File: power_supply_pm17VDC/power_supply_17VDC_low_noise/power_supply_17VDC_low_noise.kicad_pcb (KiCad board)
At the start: 2 copper layers, 87.9 x 95 mm, 36 parts, among them J1 Terminal_01x03, J2 Terminal_01x04, U1 LM317, U2 LM337, U3 LM7812, U4 LM7805

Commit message: agregando imagenes y pdf
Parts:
- moved C5 29.6 mm to (144.1, 91.6)
- moved D5 29.6 mm to (157.3, 93.5)
- moved R4 29.6 mm to (140.1, 131.8)
- moved R6 29.6 mm to (154.3, 102.1)
- moved RV1 29.6 mm to (150.8, 124.1)
- moved RV2 29.6 mm to (139.5, 92.0)
- moved U1 29.6 mm to (135.3, 102.5)
- moved U2 29.6 mm to (135.3, 124.1)
- moved U3 29.6 mm to (135.3, 76.1)
- moved C1 29.6 mm to (114.8, 98.3)
- moved C11 29.6 mm to (133.8, 56.4)
- moved C12 29.6 mm to (137.7, 64.6)
- moved C2 29.6 mm to (113.8, 125.7)
- moved C3 29.6 mm to (125.6, 97.1)
- moved C4 29.6 mm to (124.2, 116.5)
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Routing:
- net GND: track 392.8 -> 395.5 mm
- net Net-(D8-A): track 11.0 -> 13.1 mm
- net Net-(D2-K): track 71.8 -> 72.8 mm

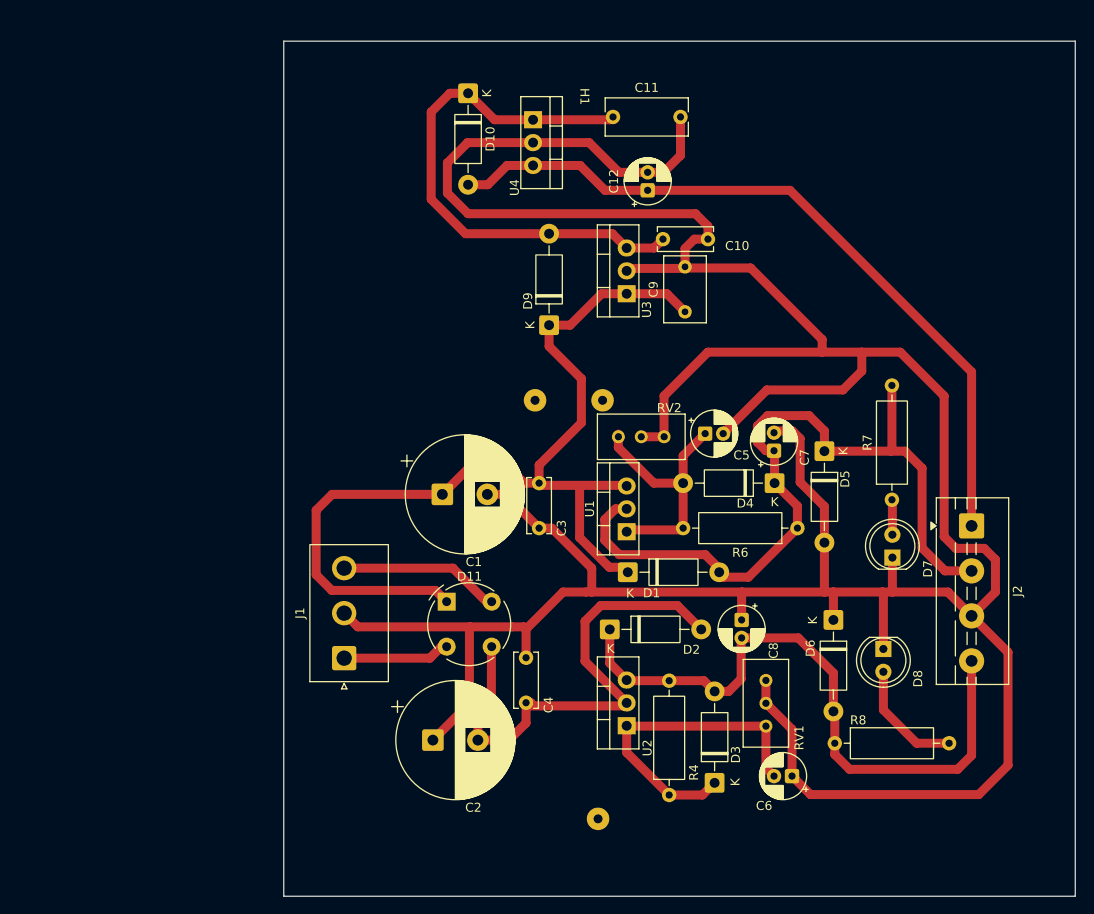
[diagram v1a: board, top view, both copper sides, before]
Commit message: finalizado STM y fuente de poder limpia, todo conforme a las huellas.
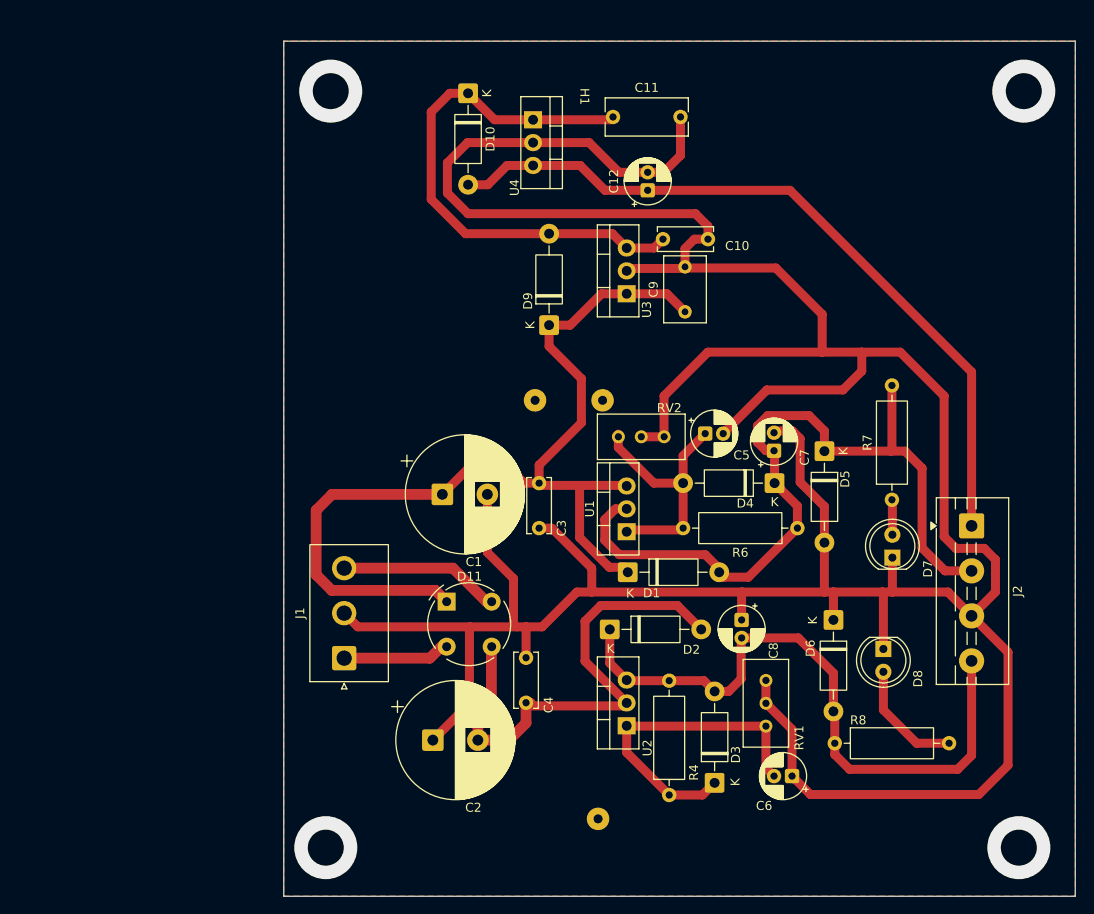
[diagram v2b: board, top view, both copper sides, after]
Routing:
- net GND: track 395.5 -> 405.5 mm
- net (no net): vias 0 -> 4
- added copper zone on F.Cu, net GND
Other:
- board text added: "mDamian 02/2026"
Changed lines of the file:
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@@
 		(layer "Margin")
+	)
+	(gr_text "mDamian 02/2026\n\n"
+		(at 105.3 84.1 0)
+		(layer "B.SilkS")
+		(effects
+			(font
+				(size 1 1)
+				(thickness 0.1)
+			)
+			(justify left bottom)
+		)
+	)
+	(gr_text "mDamian 02/2026\n\n"
+		(at 119.6 79.2 0)
+		(layer "B.SilkS")
+		(effects
+			(font
+				(size 1 1)
+				(thickness 0.1)
+			)
+			(justify left bottom mirror)
+		)
+	)
+	(via
+		(at 178.9 137.6)
+		(size 7)
+		(drill 4)
+		(layers "F.Cu" "B.Cu")
+		(net 0)
+	)
+	(via
+		(at 179.45 53.55)
+		(size 7)
+		(drill 4)
+		(layers "F.Cu" "B.Cu")
+		(net 0)
+	)
+	(via
+		(at 102.45 53.55)
+		(size 7)
+		(drill 4)
+		(layers "F.Cu" "B.Cu")
+		(net 0)
+	)
+	(via
+		(at 101.9 137.6)
+		(size 7)
+		(drill 4)
+		(layers "F.Cu" "B.Cu")
+		(net 0)
 	)
 	(segment
@@
 	)
 	(segment
-		(start 149.1 73.2)
-		(end 157.05 81.15)
-		(width 1)
-		(layer "F.Cu")
-		(net 1)
-	)
-	(segment
-		(start 128.27 109.2)
-		(end 130.8 109.2)
-		(width 1)
-		(layer "F.Cu")
-		(net 1)
-	)
-	(segment
 		(start 131.45 109.2)
 		(end 148.15 109.2)
@@
 	)
 	(segment
-		(start 141.940112 73.2)
-		(end 149.1 73.2)
-		(width 1)
-		(layer "F.Cu")
-		(net 1)
-	)
-	(segment
 		(start 153.7 129.65)
 		(end 155.75 131.7)
@@
 	)
 	(segment
+		(start 141.810112 73.07)
+		(end 141.940112 73.2)
+		(width 1)
+		(layer "F.Cu")
+		(net 1)
+	)
+	(segment
 		(start 151.7 91.5)
 		(end 151.9 91.3)
@@
 	)
 	(segment
-		(start 124.15 116.5)
-		(end 124.15 113.32)
-		(width 1)
-		(layer "F.Cu")
-		(net 1)
-	)
-	(segment
-		(start 130.8 109.2)
-		(end 131.45 109.2)
+		(start 157.05 78.35)
+		(end 157.05 82.55)
+		(width 1)
+		(layer "F.Cu")
+		(net 1)
+	)
+	(segment
+		(start 141.940112 73.2)
+		(end 151.9 73.2)
 		(width 1)
 		(layer "F.Cu")
@@
 	)
 	(segment
-		(start 117.910112 113.07)
-		(end 122.610112 113.07)
-		(width 1)
-		(layer "F.Cu")
-		(net 1)
-	)
-	(segment
 		(start 137.245 91.95)
 		(end 139.48 91.95)
@@
 	)
 	(segment
+		(start 129.8 109.2)
+		(end 131.45 109.2)
+		(width 1)
+		(layer "F.Cu")
+		(net 1)
+	)
+	(segment
 		(start 139.48 87.42)
 		(end 144.35 82.55)
@@
 	)
 	(segment
-		(start 141.810112 73.07)
-		(end 141.940112 73.2)
+		(start 124.15 113.07)
+		(end 125.93 113.07)
 		(width 1)
 		(layer "F.Cu")
@@
 	)
 	(segment
-		(start 124.15 113.32)
-		(end 123.9 113.07)
+		(start 117.910112 113.07)
+		(end 123.1 113.07)
+		(width 1)
+		(layer "F.Cu")
+		(net 1)
+	)
+	(segment
+		(start 122.75 107.7)
+		(end 122.75 112.72)
 		(width 1)
 		(layer "F.Cu")
@@
 	)
 	(segment
+		(start 123.1 113.07)
+		(end 124.15 113.07)
+		(width 1)
+		(layer "F.Cu")
+		(net 1)
+	)
+	(segment
 		(start 144.35 82.55)
 		(end 157.05 82.55)
@@
 	)
 	(segment
-		(start 119.85 98.35)
-		(end 121.85 98.35)
-		(width 1)
-		(layer "F.Cu")
-		(net 1)
-	)
-	(segment
-		(start 124.15 113.32)
-		(end 128.27 109.2)
-		(width 1)
-		(layer "F.Cu")
-		(net 1)
-	)
-	(segment
 		(start 131.45 106.55)
 		(end 131.45 109.2)
@@
 	)
 	(segment
-		(start 121.85 98.35)
-		(end 125.6 102.1)
-		(width 1)
-		(layer "F.Cu")
-		(net 1)
-	)
-	(segment
 		(start 155.75 131.7)
 		(end 174.45 131.7)
@@
 	)
 	(segment
-		(start 122.610112 113.07)
-		(end 123.9 113.07)
+		(start 119.85 98.35)
+		(end 119.85 104.8)
 		(width 1)
 		(layer "F.Cu")
@@
 	)
 	(segment
-		(start 157.05 81.15)
-		(end 157.05 82.55)
-		(width 1)
-		(layer "F.Cu")
-		(net 1)
-	)
-	(segment
 		(start 163.85 109.3)
 		(end 163.75 109.2)
@@
 	)
 	(segment
+		(start 124.15 116.5)
+		(end 124.15 113.07)
+		(width 1)
+		(layer "F.Cu")
+		(net 1)
+	)
+	(segment
 		(start 170.6 103.05)
 		(end 171.9 104.35)
@@
 	)
 	(segment
+		(start 119.85 104.8)
+		(end 122.75 107.7)
+		(width 1)
+		(layer "F.Cu")
+		(net 1)
+	)
+	(segment
 		(start 148.15 109.2)
 		(end 157.3 109.2)
@@
 	)
 	(segment
+		(start 125.93 113.07)
+		(end 129.8 109.2)
+		(width 1)
+		(layer "F.Cu")
+		(net 1)
+	)
+	(segment
 		(start 141.810112 73.07)
 		(end 141.810112 71.039888)
@@
 	)
 	(segment
+		(start 151.9 73.2)
+		(end 157.05 78.35)
+		(width 1)
+		(layer "F.Cu")
+		(net 1)
+	)
+	(segment
 		(start 159.35 86.75)
 		(end 161.45 84.65)
@@
 		(start 100.829887 100.120113)
 		(end 102.6 98.35)
-		(width 1)
+		(width 1.2)
 		(layer "F.Cu")
 		(net 2)
@@
 		(start 100.829887 107.279887)
 		(end 100.829887 100.120113)
-		(width 1)
+		(width 1.2)
 		(layer "F.Cu")
 		(net 2)
@@
 		(start 115.329887 110.27)
 		(end 114.079887 109.02)
-		(width 1)
+		(width 1.2)
 		(layer "F.Cu")
 		(net 2)
@@
 		(start 102.6 98.35)
 		(end 114.85 98.35)
-		(width 1)
+		(width 1.2)
 		(layer "F.Cu")
 		(net 2)
@@
 		(start 114.079887 109.02)
 		(end 102.57 109.02)
-		(width 1)
+		(width 1.2)
 		(layer "F.Cu")
 		(net 2)
@@
 		(start 102.57 109.02)
 		(end 100.829887 107.279887)
-		(width 1)
+		(width 1.2)
 		(layer "F.Cu")
 		(net 2)
@@
 		(start 120.3 121.95)
 		(end 118.8 123.45)
-		(width 1)
+		(width 1.2)
 		(layer "F.Cu")
 		(net 3)
@@
 		(start 124.15 123.75)
 		(end 124.15 121.5)
-		(width 1)
+		(width 1.2)
 		(layer "F.Cu")
 		(net 3)
@@
 		(start 120.329887 115.27)
 		(end 120.3 115.299887)
-		(width 1)
+		(width 1.2)
 		(layer "F.Cu")
 		(net 3)
@@
 		(start 118.8 125.65)
 		(end 122.25 125.65)
-		(width 1)
+		(width 1.2)
 		(layer "F.Cu")
 		(net 3)
@@
 		(start 120.3 115.299887)
 		(end 120.3 121.95)
-		(width 1)
+		(width 1.2)
 		(layer "F.Cu")
 		(net 3)
@@
 		(start 118.8 123.45)
 		(end 118.8 125.65)
-		(width 1)
+		(width 1.2)
 		(layer "F.Cu")
 		(net 3)
@@
 		(start 122.25 125.65)
 		(end 124.15 123.75)
-		(width 1)
+		(width 1.2)
 		(layer "F.Cu")
 		(net 3)
@@
 		(start 103.943637 116.5475)
 		(end 113.466137 116.5475)
-		(width 1)
+		(width 1.2)
 		(layer "F.Cu")
 		(net 12)
@@
 		(start 114.743637 115.27)
 		(end 115.329887 115.27)
-		(width 1)
+		(width 1.2)
 		(layer "F.Cu")
 		(net 12)
@@
 		(start 113.466137 116.5475)
 		(end 114.743637 115.27)
-		(width 1)
+		(width 1.2)
 		(layer "F.Cu")
 		(net 12)
@@
 		(start 116.021137 106.5475)
 		(end 119.743637 110.27)
-		(width 1)
+		(width 1.2)
 		(layer "F.Cu")
 		(net 13)
@@
 		(start 103.943637 106.5475)
 		(end 116.021137 106.5475)
-		(width 1)
+		(width 1.2)
 		(layer "F.Cu")
 		(net 13)
@@
 		(start 119.743637 110.27)
 		(end 120.329887 110.27)
-		(width 1)
+		(width 1.2)
 		(layer "F.Cu")
 		(net 13)
 	)
+	(zone
+		(net 1)
+		(net_name "GND")
+		(layer "F.Cu")
+		(hatch edge 0.5)
+		(connect_pads
+			(clearance 0.75)
+		)
+		(min_thickness 0.25)
+		(filled_areas_thickness no)
+		(fill yes
+			(thermal_gap 0.5)
+			(thermal_bridge_width 0.5)
+		)
+		(polygon
+			(pts
+				(xy 97.230225 48) (xy 97.230225 143) (xy 185.169775 143) (xy 185.169775 48)
+			)
+		)
+	)
 	(embedded_fonts no)

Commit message: Corrigiendo pcbs de fuente de poder
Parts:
- C1, C2: footprint Capacitor_THT:CP_Radial_D13.0mm_P5.00mm -> Capacitor_THT:CP_Radial_D18.0mm_P7.50mm
- moved C1 7.72 mm to (109.0, 93.2)
- moved RV2 6.50 mm to (138.6, 85.5), turned to 90 degrees
- moved C2 5.82 mm to (112.9, 131.4)
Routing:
- net Net-(D11--): track 57.5 -> 69.6 mm
- net GND: track 405.5 -> 413.9 mm
- net Net-(D1-K): track 111.8 -> 117.1 mm
- net Net-(D4-A): track 28.6 -> 27.2 mm

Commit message: chore: aplicar .gitignore y limpiar los archivos temporales de kiCad
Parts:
- added J3: Screw_Terminal_01x02, TerminalBlock_Phoenix:TerminalBlock_Phoenix_MKDS-1,5-2_1x02_P5.00mm_Horizontal, F.Cu at (174.1, 104.7)
- J1: footprint Connector_JST:JST_NV_B03P-NV_1x03_P5.00mm_Vertical -> TerminalBlock_Phoenix:TerminalBlock_Phoenix_MKDS-1,5-3_1x03_P5.00mm_Horizontal
- J2: value Terminal_01x04 -> Screw_Terminal_01x02; footprint TerminalBlock:TerminalBlock_MaiXu_MX126-5.0-04P_1x04_P5.00mm -> TerminalBlock_Phoenix:TerminalBlock_Phoenix_MKDS-1,5-2_1x02_P5.00mm_Horizontal
- moved J2 15.1 mm to (173.7, 116.9), turned to 90 degrees
- moved J1 10.00 mm to (103.9, 106.5), turned to -90 degrees
- moved C3 1.60 mm to (124.0, 97.1)
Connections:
- D11 pad 2: Net-(J1-Pin_1) -> Net-(J1-Pin_3)
- D11 pad 4: Net-(J1-Pin_3) -> Net-(J1-Pin_1)
- J2 pad 1: Net-(D10-A) -> Net-(D2-K)
- J2 pad 2: Net-(D1-A) -> GND
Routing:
- net Net-(J1-Pin_3): track 17.9 -> 11.9 mm
- net Net-(J1-Pin_1): track 11.9 -> 17.9 mm
- net GND: track 413.9 -> 418.9 mm
- net Net-(D10-A): track 83.4 -> 81.0 mm
- net Net-(D1-A): track 89.8 -> 87.7 mm
- added copper zone on B.Cu, net GND
- removed copper zone on F.Cu, net GND
